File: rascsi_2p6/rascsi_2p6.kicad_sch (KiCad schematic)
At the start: 88 parts, among them IC1 SN74LS641-1DW, IC2 SN74LS641-1DW, IC3 SN74LS641-1DW, IC4 SN74LS641-1DW, J1 Raspberry_Pi_2_3, J2 DNP, J4 I2C Pinout, J5 DNP, J6 CONNFLY DB-25, X1 Mac, X2 Dogcow, X3 Mac, X4 Dogcow, X5 Dogcow, X6 Dogcow, X7 Pi, X8 Pi

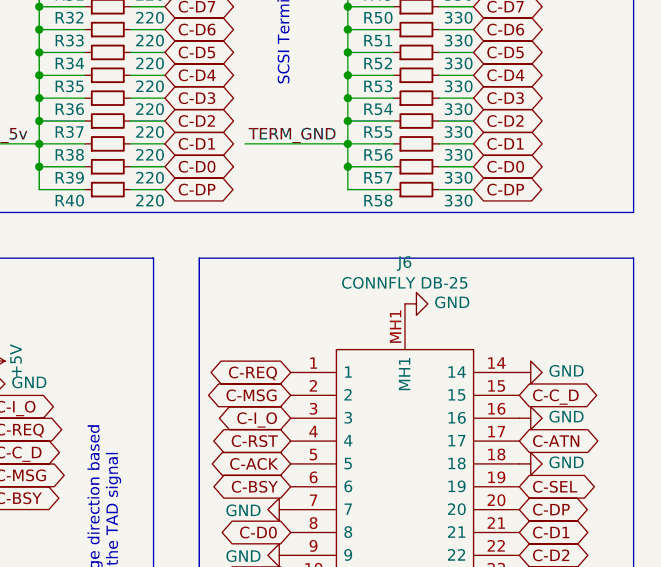
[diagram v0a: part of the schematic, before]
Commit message: Revert back to original version of rascsi 2.6 board.
This reverts commit 2b424468fa236e169660193e1614c490b0ff0ed6.
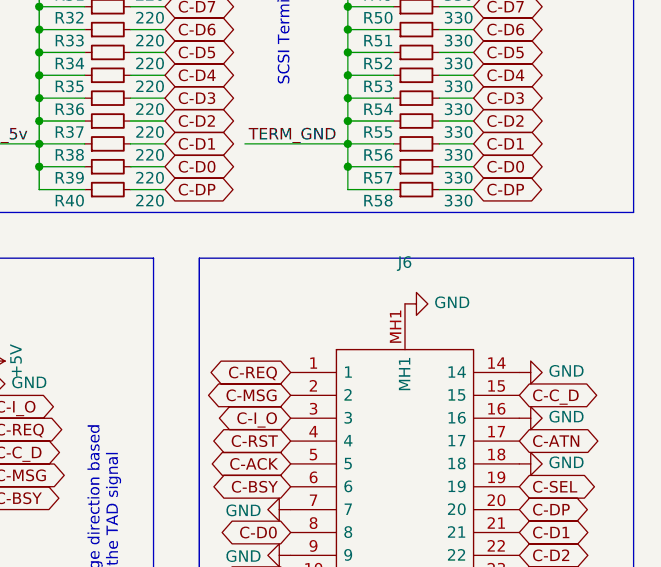
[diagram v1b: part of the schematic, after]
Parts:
- J1: LCSC C169819 -> C50982
- J6: value CONNFLY DB-25 -> (none)
- X1, X2, X3, X4, X5, X6, X7, X8: now in the parts list
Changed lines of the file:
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@@
   )
   (symbol (lib_id "SamacSys_Parts:Logo") (at 217.17 139.7 0) (unit 1)
-    (in_bom no) (on_board no)
+    (in_bom yes) (on_board yes)
     (property "Reference" "X1" (id 0) (at 213.36 137.16 0)
       (effects (font (size 1.27 1.27)) (justify left))
@@
   )
   (symbol (lib_id "SamacSys_Parts:Logo") (at 226.06 144.78 0) (unit 1)
-    (in_bom no) (on_board no)
+    (in_bom yes) (on_board yes)
     (property "Reference" "X2" (id 0) (at 222.25 142.24 0)
       (effects (font (size 1.27 1.27)) (justify left))
@@
   )
   (symbol (lib_id "SamacSys_Parts:Logo") (at 217.17 142.24 0) (unit 1)
-    (in_bom no) (on_board no)
+    (in_bom yes) (on_board yes)
     (property "Reference" "X3" (id 0) (at 213.36 139.7 0)
       (effects (font (size 1.27 1.27)) (justify left))
@@
   )
   (symbol (lib_id "SamacSys_Parts:Logo") (at 226.06 139.7 0) (unit 1)
-    (in_bom no) (on_board no)
+    (in_bom yes) (on_board yes)
     (property "Reference" "X5" (id 0) (at 222.25 137.16 0)
       (effects (font (size 1.27 1.27)) (justify left))
@@
   )
   (symbol (lib_id "SamacSys_Parts:Logo") (at 226.06 143.51 180) (unit 1)
-    (in_bom no) (on_board no)
+    (in_bom yes) (on_board yes)
     (property "Reference" "X4" (id 0) (at 222.25 144.78 0)
       (effects (font (size 1.27 1.27)) (justify right))
@@
   )
   (symbol (lib_id "SamacSys_Parts:Logo") (at 226.06 142.24 0) (unit 1)
-    (in_bom no) (on_board no)
+    (in_bom yes) (on_board yes)
     (property "Reference" "X6" (id 0) (at 222.25 139.7 0)
       (effects (font (size 1.27 1.27)) (justify left))
@@
   )
   (symbol (lib_id "SamacSys_Parts:Logo") (at 217.17 143.51 180) (unit 1)
-    (in_bom no) (on_board no)
+    (in_bom yes) (on_board yes)
     (property "Reference" "X7" (id 0) (at 213.36 144.78 0)
       (effects (font (size 1.27 1.27)) (justify right))
@@
     (in_bom yes) (on_board yes)
     (property "Reference" "J6" (id 0) (at 233.68 67.7926 90))
-    (property "Value" "CONNFLY DB-25" (id 1) (at 233.68 70.104 90))
+    (property "Value" "" (id 1) (at 233.68 70.104 90))
     (property "Footprint" "L717SDB25PA4CH4F" (id 2) (at 226.06 114.3 0)
       (effects (font (size 1.27 1.27)) (justify left) hide)
@@
   )
   (symbol (lib_id "SamacSys_Parts:Logo") (at 217.17 140.97 180) (unit 1)
-    (in_bom no) (on_board no)
+    (in_bom yes) (on_board yes)
     (property "Reference" "X8" (id 0) (at 213.36 142.24 0)
       (effects (font (size 1.27 1.27)) (justify right))
@@
       (effects (font (size 1.27 1.27)) hide)
     )
-    (property "LCSC" "C169819" (id 4) (at 49.53 113.03 0)
-      (effects (font (size 1.27 1.27)) hide)
-    )
+    (property "LCSC" "C50982" (id 4) (at 49.53 113.03 0)
+      (effects (font (size 1.27 1.27)) hide)
+    )

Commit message: update silkscreen to say piscsi and regenerate prod files
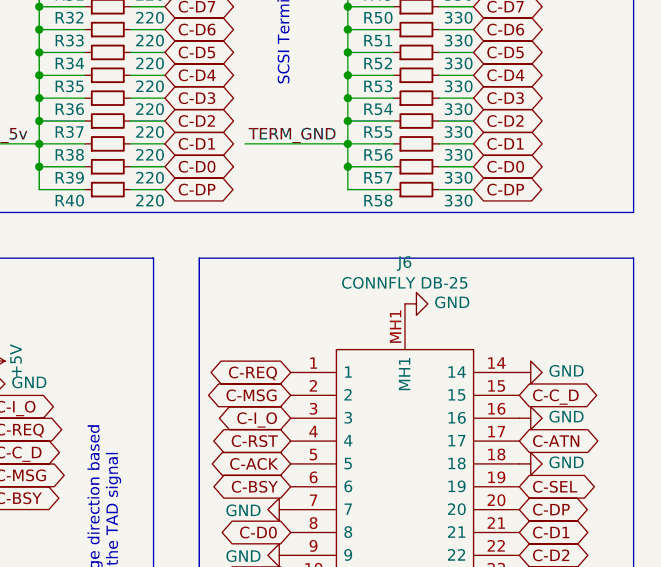
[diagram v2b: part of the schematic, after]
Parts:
- J1: LCSC C50982 -> C169819
- J6: value (none) -> CONNFLY DB-25
- X1, X2, X3, X4, X5, X6, X7, X8: now left out of the parts list
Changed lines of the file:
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@@
   )
   (symbol (lib_id "SamacSys_Parts:Logo") (at 217.17 139.7 0) (unit 1)
-    (in_bom yes) (on_board yes)
+    (in_bom no) (on_board no)
     (property "Reference" "X1" (id 0) (at 213.36 137.16 0)
       (effects (font (size 1.27 1.27)) (justify left))
@@
   )
   (symbol (lib_id "SamacSys_Parts:Logo") (at 226.06 144.78 0) (unit 1)
-    (in_bom yes) (on_board yes)
+    (in_bom no) (on_board no)
     (property "Reference" "X2" (id 0) (at 222.25 142.24 0)
       (effects (font (size 1.27 1.27)) (justify left))
@@
   )
   (symbol (lib_id "SamacSys_Parts:Logo") (at 217.17 142.24 0) (unit 1)
-    (in_bom yes) (on_board yes)
+    (in_bom no) (on_board no)
     (property "Reference" "X3" (id 0) (at 213.36 139.7 0)
       (effects (font (size 1.27 1.27)) (justify left))
@@
   )
   (symbol (lib_id "SamacSys_Parts:Logo") (at 226.06 139.7 0) (unit 1)
-    (in_bom yes) (on_board yes)
+    (in_bom no) (on_board no)
     (property "Reference" "X5" (id 0) (at 222.25 137.16 0)
       (effects (font (size 1.27 1.27)) (justify left))
@@
   )
   (symbol (lib_id "SamacSys_Parts:Logo") (at 226.06 143.51 180) (unit 1)
-    (in_bom yes) (on_board yes)
+    (in_bom no) (on_board no)
     (property "Reference" "X4" (id 0) (at 222.25 144.78 0)
       (effects (font (size 1.27 1.27)) (justify right))
@@
   )
   (symbol (lib_id "SamacSys_Parts:Logo") (at 226.06 142.24 0) (unit 1)
-    (in_bom yes) (on_board yes)
+    (in_bom no) (on_board no)
     (property "Reference" "X6" (id 0) (at 222.25 139.7 0)
       (effects (font (size 1.27 1.27)) (justify left))
@@
   )
   (symbol (lib_id "SamacSys_Parts:Logo") (at 217.17 143.51 180) (unit 1)
-    (in_bom yes) (on_board yes)
+    (in_bom no) (on_board no)
     (property "Reference" "X7" (id 0) (at 213.36 144.78 0)
       (effects (font (size 1.27 1.27)) (justify right))
@@
     (in_bom yes) (on_board yes)
     (property "Reference" "J6" (id 0) (at 233.68 67.7926 90))
-    (property "Value" "" (id 1) (at 233.68 70.104 90))
+    (property "Value" "CONNFLY DB-25" (id 1) (at 233.68 70.104 90))
     (property "Footprint" "L717SDB25PA4CH4F" (id 2) (at 226.06 114.3 0)
       (effects (font (size 1.27 1.27)) (justify left) hide)
@@
   )
   (symbol (lib_id "SamacSys_Parts:Logo") (at 217.17 140.97 180) (unit 1)
-    (in_bom yes) (on_board yes)
+    (in_bom no) (on_board no)
     (property "Reference" "X8" (id 0) (at 213.36 142.24 0)
       (effects (font (size 1.27 1.27)) (justify right))
@@
       (effects (font (size 1.27 1.27)) hide)
     )
-    (property "LCSC" "C50982" (id 4) (at 49.53 113.03 0)
-      (effects (font (size 1.27 1.27)) hide)
-    )
+    (property "LCSC" "C169819" (id 4) (at 49.53 113.03 0)
+      (effects (font (size 1.27 1.27)) hide)
+    )
